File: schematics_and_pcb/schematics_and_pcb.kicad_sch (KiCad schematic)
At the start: 59 parts, among them J1 RND 205-00623, J2 RND 205-00627, SW1 RND 210-00210, U1 MIC5235YM5-TR, U2 AP2125N-3.3TRG1, U3 PWM3389DM-T3QU, U4 STM32F411RETx, Y1 YLFXTAL029370

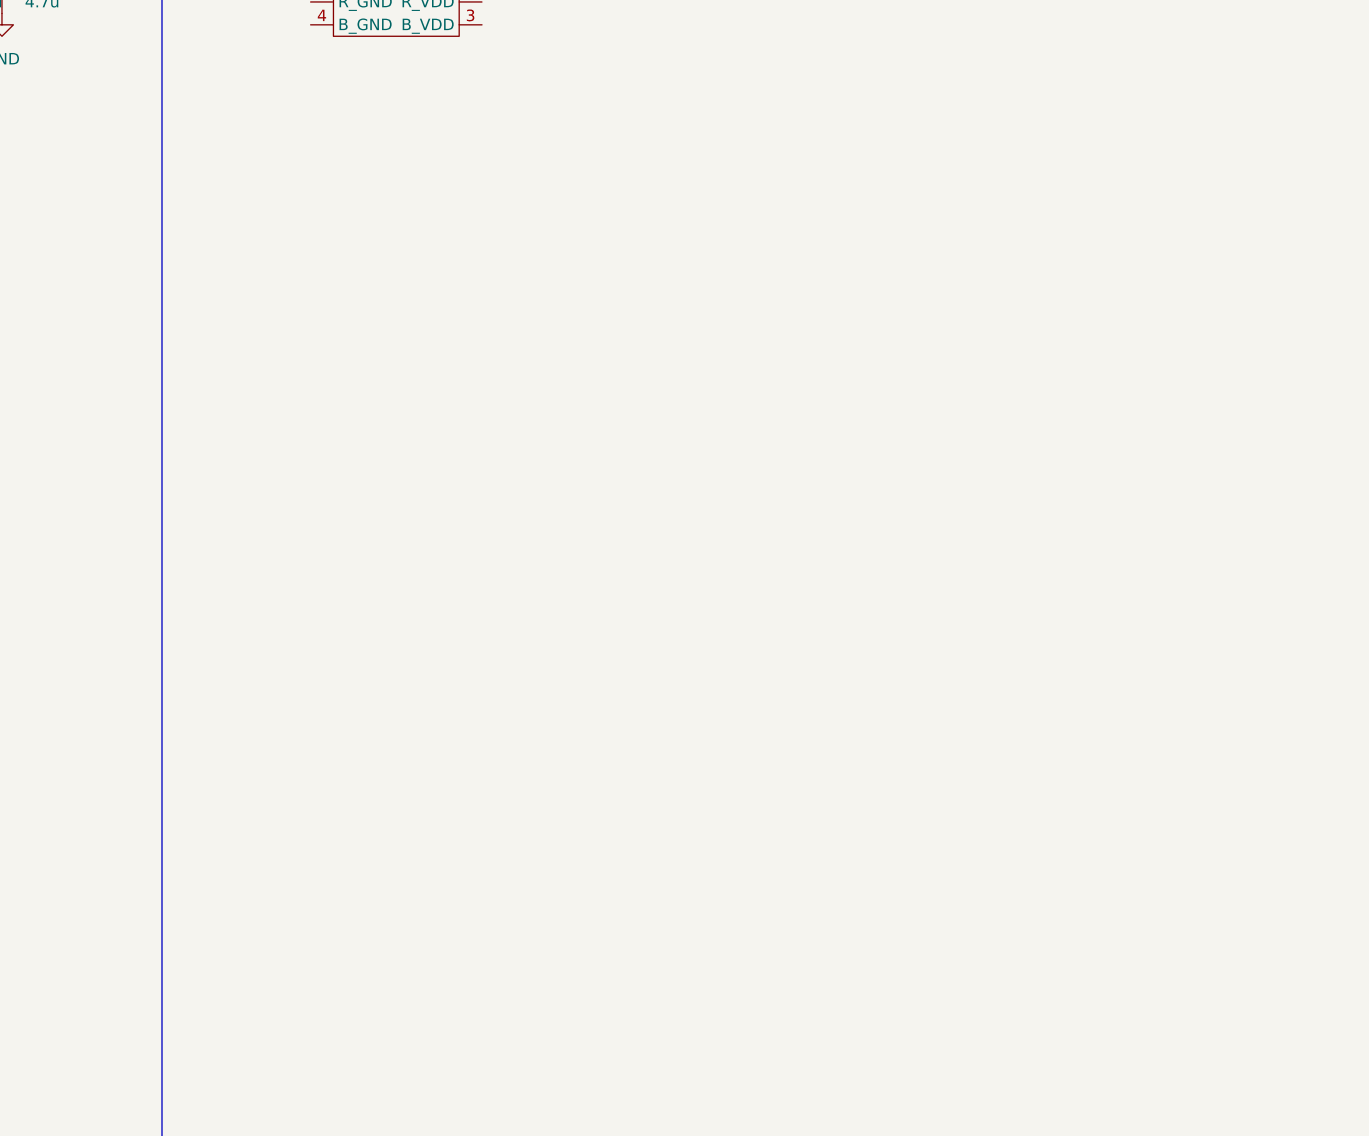
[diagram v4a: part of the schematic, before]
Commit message: Added a possible motor drive to schematic.
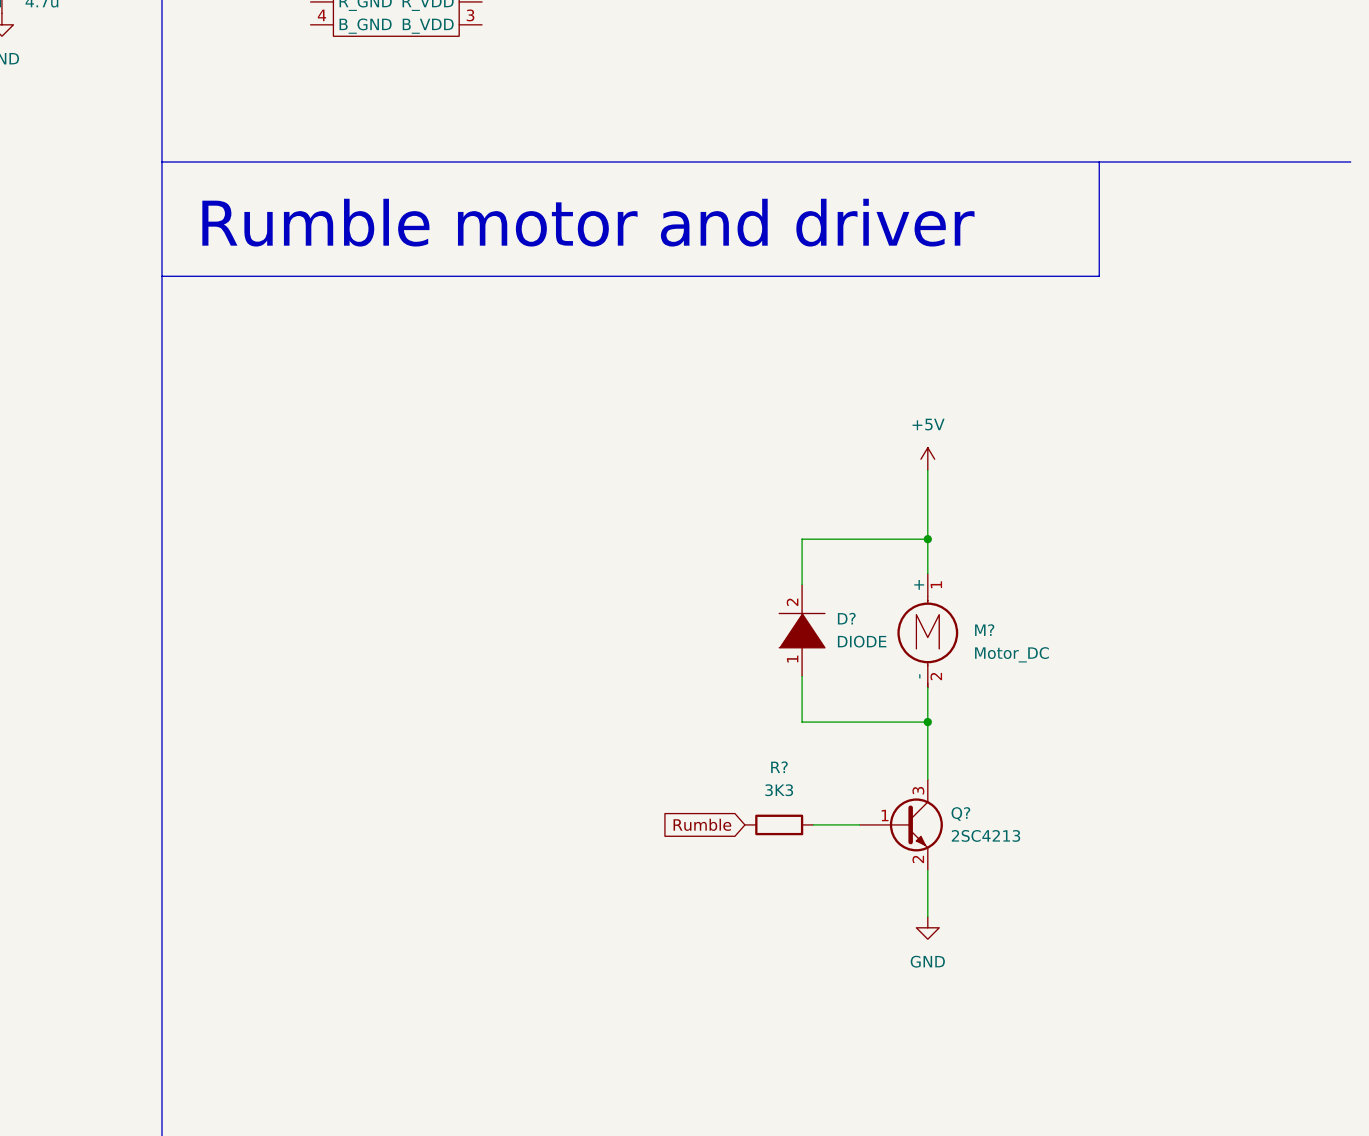
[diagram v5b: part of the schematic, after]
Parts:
- added D?: DIODE, symbol pspice:DIODE
- added M?: Motor_DC, symbol Motor:Motor_DC
- added Q?: 2SC4213, Package_TO_SOT_SMD:SOT-323_SC-70, symbol Transistor_BJT:2SC4213
- added R?: 3K3, symbol Device:R
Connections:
- net +5V: now also D?.2 (A), M?.1 (+)
- net GND: now also Q?.2 (E)
- new net: D?.1 (K), M?.2 (-), Q?.3 (C)
- new net: Q?.1 (B), R?.2
- new net Rumble: R?.1
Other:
- note added: "Rumble motor and driver"
